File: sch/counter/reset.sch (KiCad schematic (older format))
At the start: 22 parts, among them Q33 Q_NMOS_GSD

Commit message: Counter schematic improvements
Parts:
- removed JP5: SolderJumper_2_Bridged, symbol Jumper:SolderJumper_2_Bridged
- removed JP6: SolderJumper_2_Open, symbol Jumper:SolderJumper_2_Open
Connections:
- net at D85.2 (A), D86.2 (A), D87.2 (A)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: now also D93.2 (A), D94.2 (A), D95.2 (A), D96.2 (A), Q33.1 (G), R37.2
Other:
- note added: "Do not install if fixed reset value is used"
- note added: "Install only four diodes selecting the reset constant.\nDo not install if jumper selection is used."
- moved on the sheet: D85, D86, D87, D88, D89, D90, D91, D92, D93, D94, D95, D96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

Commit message: One flip-flop is placed on PCB
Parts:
- D85, D86, D87, D88, D89, D90, D91, D92, D93, D94, D95, D96, D97, D98: footprint (none) -> Diode_SMD:D_MiniMELF
- JP1, JP2, JP3, JP4: footprint (none) -> Connector_PinHeader_2.54mm:PinHeader_1x03_P2.54mm_Vertical
- Q33: footprint (none) -> Package_TO_SOT_SMD:SOT-23
- R37: footprint (none) -> Resistor_SMD:R_0805_2012Metric
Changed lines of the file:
@@
 EESchema Schematic File Version 4
+LIBS:counter-cache
 EELAYER 26 0
 EELAYER END
@@
 F 0 "D85" H 5250 1500 50  0000 C CNN
 F 1 "D" H 5600 1625 50  0001 C CNN
-F 2 "" H 5600 1500 50  0001 C CNN
+F 2 "Diode_SMD:D_MiniMELF" H 5600 1500 50  0001 C CNN
 F 3 "~" H 5600 1500 50  0001 C CNN
 	1    5600 1500
@@
 F 0 "D86" H 5250 1650 50  0000 C CNN
 F 1 "D" H 5600 1775 50  0001 C CNN
-F 2 "" H 5600 1650 50  0001 C CNN
+F 2 "Diode_SMD:D_MiniMELF" H 5600 1650 50  0001 C CNN
 F 3 "~" H 5600 1650 50  0001 C CNN
 	1    5600 1650
@@
 F 0 "D87" H 5250 1800 50  0000 C CNN
 F 1 "D" H 5600 1925 50  0001 C CNN
-F 2 "" H 5600 1800 50  0001 C CNN
+F 2 "Diode_SMD:D_MiniMELF" H 5600 1800 50  0001 C CNN
 F 3 "~" H 5600 1800 50  0001 C CNN
 	1    5600 1800
@@
 F 0 "D88" H 5250 1950 50  0000 C CNN
 F 1 "D" H 5600 2075 50  0001 C CNN
-F 2 "" H 5600 1950 50  0001 C CNN
+F 2 "Diode_SMD:D_MiniMELF" H 5600 1950 50  0001 C CNN
 F 3 "~" H 5600 1950 50  0001 C CNN
 	1    5600 1950
@@
 F 0 "D89" H 5250 2100 50  0000 C CNN
 F 1 "D" H 5600 2225 50  0001 C CNN
-F 2 "" H 5600 2100 50  0001 C CNN
+F 2 "Diode_SMD:D_MiniMELF" H 5600 2100 50  0001 C CNN
 F 3 "~" H 5600 2100 50  0001 C CNN
 	1    5600 2100
@@
 F 0 "D90" H 5250 2250 50  0000 C CNN
 F 1 "D" H 5600 2375 50  0001 C CNN
-F 2 "" H 5600 2250 50  0001 C CNN
+F 2 "Diode_SMD:D_MiniMELF" H 5600 2250 50  0001 C CNN
 F 3 "~" H 5600 2250 50  0001 C CNN
 	1    5600 2250
@@
 F 0 "D91" H 5250 2400 50  0000 C CNN
 F 1 "D" H 5600 2525 50  0001 C CNN
-F 2 "" H 5600 2400 50  0001 C CNN
+F 2 "Diode_SMD:D_MiniMELF" H 5600 2400 50  0001 C CNN
 F 3 "~" H 5600 2400 50  0001 C CNN
 	1    5600 2400
@@
 F 0 "D92" H 5250 2550 50  0000 C CNN
 F 1 "D" H 5600 2675 50  0001 C CNN
-F 2 "" H 5600 2550 50  0001 C CNN
+F 2 "Diode_SMD:D_MiniMELF" H 5600 2550 50  0001 C CNN
 F 3 "~" H 5600 2550 50  0001 C CNN
 	1    5600 2550
@@
 F 0 "R37" H 6120 1546 50  0000 L CNN
 F 1 "20k" H 6120 1455 50  0000 L CNN
-F 2 "" V 5980 1500 50  0001 C CNN
+F 2 "Resistor_SMD:R_0805_2012Metric" V 5980 1500 50  0001 C CNN
 F 3 "~" H 6050 1500 50  0001 C CNN
 	1    6050 1500
@@
 F 0 "D97" H 6450 1850 50  0000 C CNN
 F 1 "D" H 6500 1875 50  0001 C CNN
-F 2 "" H 6500 1750 50  0001 C CNN
+F 2 "Diode_SMD:D_MiniMELF" H 6500 1750 50  0001 C CNN
 F 3 "~" H 6500 1750 50  0001 C CNN
 	1    6500 1750
@@
 F 0 "D98" V 6550 1500 50  0000 C CNN
 F 1 "D" H 6650 1725 50  0001 C CNN
-F 2 "" H 6650 1600 50  0001 C CNN
+F 2 "Diode_SMD:D_MiniMELF" H 6650 1600 50  0001 C CNN
 F 3 "~" H 6650 1600 50  0001 C CNN
 	1    6650 1600
@@
 F 0 "JP2" V 5750 4000 50  0000 L CNN
 F 1 "Jumper_3_Open" V 5555 3986 50  0001 L CNN
-F 2 "" H 5600 3900 50  0001 C CNN
+F 2 "Connector_PinHeader_2.54mm:PinHeader_1x03_P2.54mm_Vertical" H 5600 3900 50  0001 C CNN
 F 3 "~" H 5600 3900 50  0001 C CNN
 	1    5600 3900
@@
 F 0 "D94" H 5900 4000 50  0000 C CNN
 F 1 "D" H 5900 4025 50  0001 C CNN
-F 2 "" H 5900 3900 50  0001 C CNN
+F 2 "Diode_SMD:D_MiniMELF" H 5900 3900 50  0001 C CNN
 F 3 "~" H 5900 3900 50  0001 C CNN
 	1    5900 3900
@@
 F 0 "JP1" V 5750 3300 50  0000 L CNN
 F 1 "Jumper_3_Open" V 5555 3286 50  0001 L CNN
-F 2 "" H 5600 3200 50  0001 C CNN
+F 2 "Connector_PinHeader_2.54mm:PinHeader_1x03_P2.54mm_Vertical" H 5600 3200 50  0001 C CNN
 F 3 "~" H 5600 3200 50  0001 C CNN
 	1    5600 3200
@@
 F 0 "D93" H 5900 3300 50  0000 C CNN
 F 1 "D" H 5900 3325 50  0001 C CNN
-F 2 "" H 5900 3200 50  0001 C CNN
+F 2 "Diode_SMD:D_MiniMELF" H 5900 3200 50  0001 C CNN
 F 3 "~" H 5900 3200 50  0001 C CNN
 	1    5900 3200
@@
 F 0 "JP3" V 5750 4800 50  0000 L CNN
 F 1 "Jumper_3_Open" V 5555 4786 50  0001 L CNN
-F 2 "" H 5600 4700 50  0001 C CNN
+F 2 "Connector_PinHeader_2.54mm:PinHeader_1x03_P2.54mm_Vertical" H 5600 4700 50  0001 C CNN
 F 3 "~" H 5600 4700 50  0001 C CNN
 	1    5600 4700
@@
 F 0 "D95" H 5900 4800 50  0000 C CNN
 F 1 "D" H 5900 4825 50  0001 C CNN
-F 2 "" H 5900 4700 50  0001 C CNN
+F 2 "Diode_SMD:D_MiniMELF" H 5900 4700 50  0001 C CNN
 F 3 "~" H 5900 4700 50  0001 C CNN
 	1    5900 4700
@@
 F 0 "JP4" V 5750 5600 50  0000 L CNN
 F 1 "Jumper_3_Open" V 5555 5586 50  0001 L CNN
-F 2 "" H 5600 5500 50  0001 C CNN
+F 2 "Connector_PinHeader_2.54mm:PinHeader_1x03_P2.54mm_Vertical" H 5600 5500 50  0001 C CNN
 F 3 "~" H 5600 5500 50  0001 C CNN
 	1    5600 5500
@@
 F 0 "D96" H 5900 5600 50  0000 C CNN
 F 1 "D" H 5900 5625 50  0001 C CNN
-F 2 "" H 5900 5500 50  0001 C CNN
+F 2 "Diode_SMD:D_MiniMELF" H 5900 5500 50  0001 C CNN
 F 3 "~" H 5900 5500 50  0001 C CNN
 	1    5900 5500
@@
 F 0 "Q33" H 6455 1996 50  0000 L CNN
 F 1 "Q_NMOS_GSD" H 6455 1905 50  0000 L CNN
-F 2 "" H 6450 2050 50  0001 C CNN
+F 2 "Package_TO_SOT_SMD:SOT-23" H 6450 2050 50  0001 C CNN
 F 3 "~" H 6250 1950 50  0001 C CNN
 	1    6250 1950

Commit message: The counter board is complete
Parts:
- removed D93, D94, D95, D96: D, Diode_SMD:D_MiniMELF, symbol Device:D
- removed JP1, JP2, JP3, JP4: Jumper_3_Open, Connector_PinHeader_2.54mm:PinHeader_1x03_P2.54mm_Vertical, symbol Jumper:Jumper_3_Open
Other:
- note added: "Install only four diodes selecting the reset constant."
- note removed: "Do not install if fixed reset value is used"
- note removed: "Install only four diodes selecting the reset constant.\nDo not install if jumper selection is used."
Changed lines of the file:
@@
 Wire Wire Line
 	6050 1950 6050 1650
-$Comp
-L Jumper:Jumper_3_Open JP2
-U 1 1 5BF758E7
-P 5600 3900
-F 0 "JP2" V 5750 4000 50  0000 L CNN
-F 1 "Jumper_3_Open" V 5555 3986 50  0001 L CNN
-F 2 "Connector_PinHeader_2.54mm:PinHeader_1x03_P2.54mm_Vertical" H 5600 3900 50  0001 C CNN
-F 3 "~" H 5600 3900 50  0001 C CNN
-	1    5600 3900
-	0    -1   -1   0
-$EndComp
-$Comp
-L Device:D D?
-U 1 1 5BF759D9
-P 5900 3900
-AR Path="/5BF759D9" Ref="D?"  Part="1"
-AR Path="/5BF5D665/5BF759D9" Ref="D94"  Part="1"
-F 0 "D94" H 5900 4000 50  0000 C CNN
-F 1 "D" H 5900 4025 50  0001 C CNN
-F 2 "Diode_SMD:D_MiniMELF" H 5900 3900 50  0001 C CNN
-F 3 "~" H 5900 3900 50  0001 C CNN
-	1    5900 3900
-	1    0    0    -1
-$EndComp
-$Comp
-L Jumper:Jumper_3_Open JP1
-U 1 1 5BF75D5C
-P 5600 3200
-F 0 "JP1" V 5750 3300 50  0000 L CNN
-F 1 "Jumper_3_Open" V 5555 3286 50  0001 L CNN
-F 2 "Connector_PinHeader_2.54mm:PinHeader_1x03_P2.54mm_Vertical" H 5600 3200 50  0001 C CNN
-F 3 "~" H 5600 3200 50  0001 C CNN
-	1    5600 3200
-	0    -1   -1   0
-$EndComp
-$Comp
-L Device:D D?
-U 1 1 5BF75D63
-P 5900 3200
-AR Path="/5BF75D63" Ref="D?"  Part="1"
-AR Path="/5BF5D665/5BF75D63" Ref="D93"  Part="1"
-F 0 "D93" H 5900 3300 50  0000 C CNN
-F 1 "D" H 5900 3325 50  0001 C CNN
-F 2 "Diode_SMD:D_MiniMELF" H 5900 3200 50  0001 C CNN
-F 3 "~" H 5900 3200 50  0001 C CNN
-	1    5900 3200
-	1    0    0    -1
-$EndComp
-$Comp
-L Jumper:Jumper_3_Open JP3
-U 1 1 5BF7604B
-P 5600 4700
-F 0 "JP3" V 5750 4800 50  0000 L CNN
-F 1 "Jumper_3_Open" V 5555 4786 50  0001 L CNN
-F 2 "Connector_PinHeader_2.54mm:PinHeader_1x03_P2.54mm_Vertical" H 5600 4700 50  0001 C CNN
-F 3 "~" H 5600 4700 50  0001 C CNN
-	1    5600 4700
-	0    -1   -1   0
-$EndComp
-$Comp
-L Device:D D?
-U 1 1 5BF76052
-P 5900 4700
-AR Path="/5BF76052" Ref="D?"  Part="1"
-AR Path="/5BF5D665/5BF76052" Ref="D95"  Part="1"
-F 0 "D95" H 5900 4800 50  0000 C CNN
-F 1 "D" H 5900 4825 50  0001 C CNN
-F 2 "Diode_SMD:D_MiniMELF" H 5900 4700 50  0001 C CNN
-F 3 "~" H 5900 4700 50  0001 C CNN
-	1    5900 4700
-	1    0    0    -1
-$EndComp
-$Comp
-L Jumper:Jumper_3_Open JP4
-U 1 1 5BF760E4
-P 5600 5500
-F 0 "JP4" V 5750 5600 50  0000 L CNN
-F 1 "Jumper_3_Open" V 5555 5586 50  0001 L CNN
-F 2 "Connector_PinHeader_2.54mm:PinHeader_1x03_P2.54mm_Vertical" H 5600 5500 50  0001 C CNN
-F 3 "~" H 5600 5500 50  0001 C CNN
-	1    5600 5500
-	0    -1   -1   0
-$EndComp
-$Comp
-L Device:D D?
-U 1 1 5BF760EB
-P 5900 5500
-AR Path="/5BF760EB" Ref="D?"  Part="1"
-AR Path="/5BF5D665/5BF760EB" Ref="D96"  Part="1"
-F 0 "D96" H 5900 5600 50  0000 C CNN
-F 1 "D" H 5900 5625 50  0001 C CNN
-F 2 "Diode_SMD:D_MiniMELF" H 5900 5500 50  0001 C CNN
-F 3 "~" H 5900 5500 50  0001 C CNN
-	1    5900 5500
-	1    0    0    -1
-$EndComp
-Connection ~ 6050 3200
-Wire Wire Line
-	6050 3200 6050 3900
-Connection ~ 6050 3900
-Wire Wire Line
-	6050 3900 6050 4700
-Connection ~ 6050 4700
-Wire Wire Line
-	6050 4700 6050 5500
-Text Label 5600 2950 2    50   ~ 0
-Q1
-Text Label 5600 3450 2    50   ~ 0
-~Q1
-Text Label 5600 3650 2    50   ~ 0
-Q2
-Text Label 5600 4150 2    50   ~ 0
-~Q2
-Text Label 5600 4450 2    50   ~ 0
-Q4
-Text Label 5600 4950 2    50   ~ 0
-~Q4
-Text Label 5600 5250 2    50   ~ 0
-Q8
-Text Label 5600 5750 2    50   ~ 0
-~Q8
 Text HLabel 950  1100 0    50   Input ~ 0
 Q1
@@
 ~RSTin
 Wire Notes Line
-	6200 2900 6400 2900
-Wire Notes Line
-	6400 2900 6400 5700
-Wire Notes Line
-	6400 5700 6200 5700
-Text Notes 6350 5150 1    50   ~ 0
-Do not install if fixed reset value is used
-Wire Notes Line
 	5100 1400 4900 1400
 Wire Notes Line
@@
 	4900 2600 5100 2600
 Text Notes 4850 2850 1    50   ~ 0
-Install only four diodes selecting the reset constant.\nDo not install if jumper selection is used.
+Install only four diodes selecting the reset constant.
 $Comp
 L Device:Q_NMOS_GSD Q?
@@
 	1    0    0    -1
 $EndComp
-Wire Wire Line
-	6050 1950 6050 3200
 Connection ~ 6050 1950
 Wire Wire Line

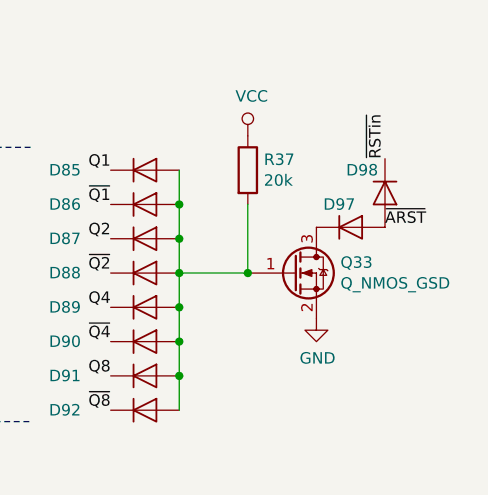
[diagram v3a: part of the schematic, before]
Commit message: Added datasheets, set component values, calculated LED resistors
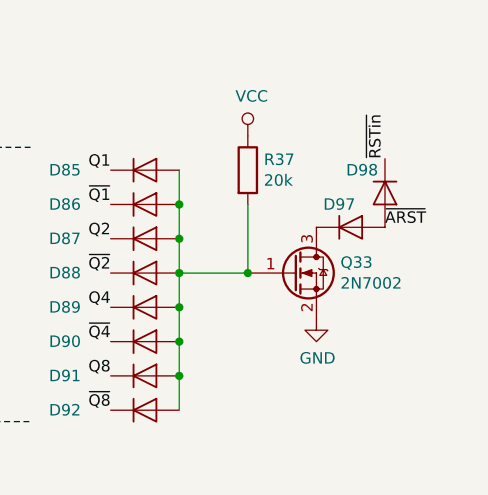
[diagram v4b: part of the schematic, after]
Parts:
- D85, D86, D87, D88, D89, D90, D91, D92, D97, D98: value D -> LL103C
- Q33: value Q_NMOS_GSD -> 2N7002
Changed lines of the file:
@@
 AR Path="/5BF5D665/5BF5E6AC" Ref="D85"  Part="1"
 F 0 "D85" H 5250 1500 50  0000 C CNN
-F 1 "D" H 5600 1625 50  0001 C CNN
+F 1 "LL103C" H 5600 1625 50  0001 C CNN
 F 2 "Diode_SMD:D_MiniMELF" H 5600 1500 50  0001 C CNN
 F 3 "~" H 5600 1500 50  0001 C CNN
@@
 AR Path="/5BF5D665/5BF5E6B3" Ref="D86"  Part="1"
 F 0 "D86" H 5250 1650 50  0000 C CNN
-F 1 "D" H 5600 1775 50  0001 C CNN
+F 1 "LL103C" H 5600 1775 50  0001 C CNN
 F 2 "Diode_SMD:D_MiniMELF" H 5600 1650 50  0001 C CNN
 F 3 "~" H 5600 1650 50  0001 C CNN
@@
 AR Path="/5BF5D665/5BF5E6BA" Ref="D87"  Part="1"
 F 0 "D87" H 5250 1800 50  0000 C CNN
-F 1 "D" H 5600 1925 50  0001 C CNN
+F 1 "LL103C" H 5600 1925 50  0001 C CNN
 F 2 "Diode_SMD:D_MiniMELF" H 5600 1800 50  0001 C CNN
 F 3 "~" H 5600 1800 50  0001 C CNN
@@
 AR Path="/5BF5D665/5BF5E6C1" Ref="D88"  Part="1"
 F 0 "D88" H 5250 1950 50  0000 C CNN
-F 1 "D" H 5600 2075 50  0001 C CNN
+F 1 "LL103C" H 5600 2075 50  0001 C CNN
 F 2 "Diode_SMD:D_MiniMELF" H 5600 1950 50  0001 C CNN
 F 3 "~" H 5600 1950 50  0001 C CNN
@@
 AR Path="/5BF5D665/5BF5E6C8" Ref="D89"  Part="1"
 F 0 "D89" H 5250 2100 50  0000 C CNN
-F 1 "D" H 5600 2225 50  0001 C CNN
+F 1 "LL103C" H 5600 2225 50  0001 C CNN
 F 2 "Diode_SMD:D_MiniMELF" H 5600 2100 50  0001 C CNN
 F 3 "~" H 5600 2100 50  0001 C CNN
@@
 AR Path="/5BF5D665/5BF5E6CF" Ref="D90"  Part="1"
 F 0 "D90" H 5250 2250 50  0000 C CNN
-F 1 "D" H 5600 2375 50  0001 C CNN
+F 1 "LL103C" H 5600 2375 50  0001 C CNN
 F 2 "Diode_SMD:D_MiniMELF" H 5600 2250 50  0001 C CNN
 F 3 "~" H 5600 2250 50  0001 C CNN
@@
 AR Path="/5BF5D665/5BF5E6D6" Ref="D91"  Part="1"
 F 0 "D91" H 5250 2400 50  0000 C CNN
-F 1 "D" H 5600 2525 50  0001 C CNN
+F 1 "LL103C" H 5600 2525 50  0001 C CNN
 F 2 "Diode_SMD:D_MiniMELF" H 5600 2400 50  0001 C CNN
 F 3 "~" H 5600 2400 50  0001 C CNN
@@
 AR Path="/5BF5D665/5BF5E6DD" Ref="D92"  Part="1"
 F 0 "D92" H 5250 2550 50  0000 C CNN
-F 1 "D" H 5600 2675 50  0001 C CNN
+F 1 "LL103C" H 5600 2675 50  0001 C CNN
 F 2 "Diode_SMD:D_MiniMELF" H 5600 2550 50  0001 C CNN
 F 3 "~" H 5600 2550 50  0001 C CNN
@@
 AR Path="/5BF5D665/5BF5E715" Ref="D97"  Part="1"
 F 0 "D97" H 6450 1850 50  0000 C CNN
-F 1 "D" H 6500 1875 50  0001 C CNN
+F 1 "LL103C" H 6500 1875 50  0001 C CNN
 F 2 "Diode_SMD:D_MiniMELF" H 6500 1750 50  0001 C CNN
 F 3 "~" H 6500 1750 50  0001 C CNN
@@
 AR Path="/5BF5D665/5BF5E71C" Ref="D98"  Part="1"
 F 0 "D98" V 6550 1500 50  0000 C CNN
-F 1 "D" H 6650 1725 50  0001 C CNN
+F 1 "LL103C" H 6650 1725 50  0001 C CNN
 F 2 "Diode_SMD:D_MiniMELF" H 6650 1600 50  0001 C CNN
 F 3 "~" H 6650 1600 50  0001 C CNN
@@
 AR Path="/5BF5D665/5BF5E707" Ref="Q33"  Part="1"
 F 0 "Q33" H 6455 1996 50  0000 L CNN
-F 1 "Q_NMOS_GSD" H 6455 1905 50  0000 L CNN
+F 1 "2N7002" H 6455 1905 50  0000 L CNN
 F 2 "Package_TO_SOT_SMD:SOT-23" H 6450 2050 50  0001 C CNN
 F 3 "~" H 6250 1950 50  0001 C CNN
